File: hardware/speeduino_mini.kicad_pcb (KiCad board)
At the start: 2 copper layers, 264.2 x 66 mm, 209 parts, among them J1 O2, J10 Injector, J11 Ignitor Pack, J12 oil pressure, J13 fuel pressure, J14 power, J15 Conn_01x08_Female, J2 Raspberry_Pi_2_3, J3 TPS, J4 IAT, J5 head temperature, J6 crankshaft position sensor, J7 Injector, J8 Injector, J9 Injector, Q1 2N7002, Q2 SQ3457EV, Q3 2N7002, Q5 SQ3457EV, U10 SN74LVC2T45MDCTTEP, U11 TLE8366, U12 LD1117S50TR_SOT223, U13 DRV103H, U14 DRV103H, U15 DRV103H, U3 ATmega2561-16AU, U4 MPX4250AP1, U5 SN74LVC2T45MDCTTEP, U7 DRV103H, U8 MCP2003B, U9 SN74LVC2T45MDCTTEP, Y1 CSTCE16M0V53-R0

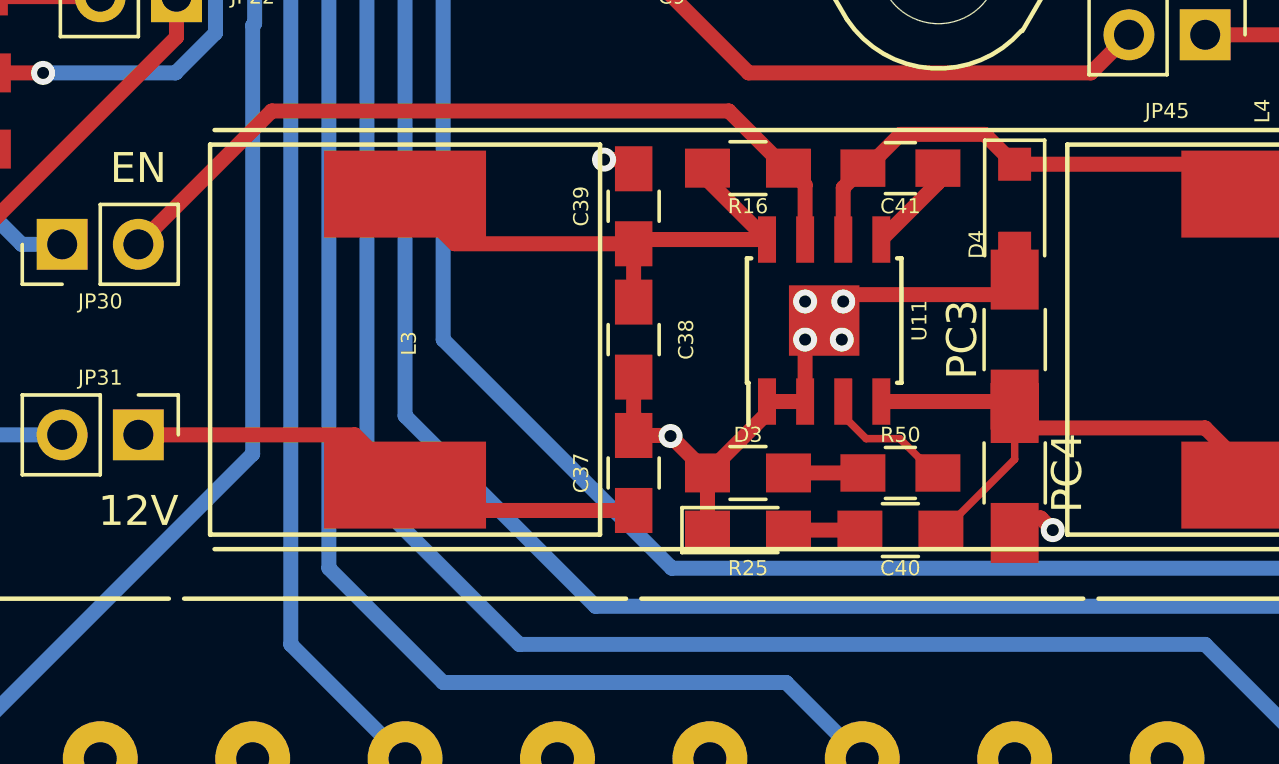
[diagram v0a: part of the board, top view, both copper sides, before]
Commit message: Moved PC3, fixed R25, D3, C40 and R50 silkscreen
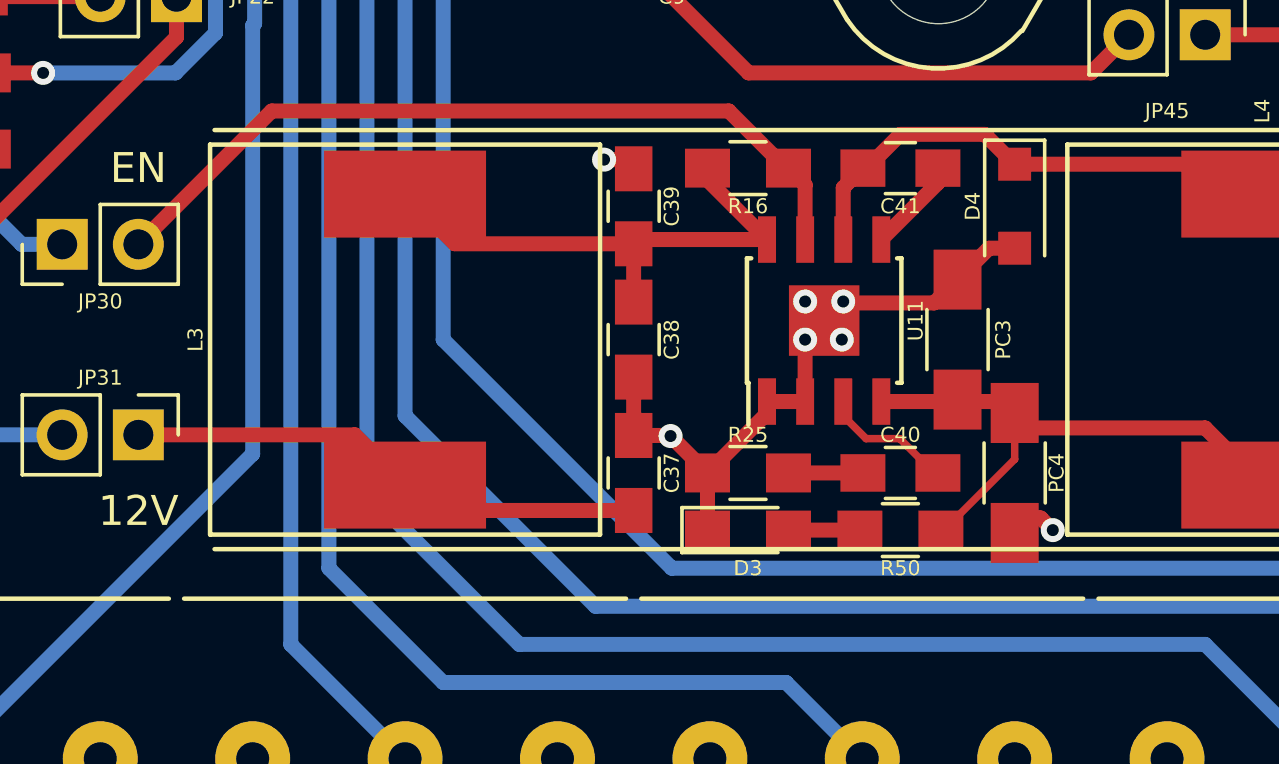
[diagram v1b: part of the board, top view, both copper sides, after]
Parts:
- moved PC3 1.91 mm to (187.3, 108.0)
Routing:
- net GND: track 329.9 -> 329.3 mm
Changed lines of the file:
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@@
     (thickness 1.6)
     (drawings 103)
-    (tracks 1155)
+    (tracks 1156)
     (zones 0)
     (modules 209)
@@
     (tags "capacitor 1206")
     (attr smd)
-    (fp_text reference PC4 (at 0 -1.75 270) (layer F.SilkS)
-      (effects (font (size 1 1) (thickness 0.15)))
+    (fp_text reference PC4 (at 0 -1.397 270) (layer F.SilkS)
+      (effects (font (size 0.5 0.5) (thickness 0.075)))
     )
     (fp_text value "47uF 10V" (at 0 2 270) (layer F.Fab)
@@
   )
   (module Capacitors_SMD:C_1206_HandSoldering (layer F.Cu)
-    (at 189.23 107.95 90)
+    (at 187.325 107.95 90)
     (descr "Capacitor SMD 1206, hand soldering")
     (tags "capacitor 1206")
     (attr smd)
-    (fp_text reference PC3 (at 0 -1.75 90) (layer F.SilkS)
-      (effects (font (size 1 1) (thickness 0.15)))
+    (fp_text reference PC3 (at 0 1.524 90) (layer F.SilkS)
+      (effects (font (size 0.5 0.5) (thickness 0.075)))
     )
     (fp_text value "47uF 10V" (at 0 2 90) (layer F.Fab)
@@
     (tags "SOIC 1.27")
     (attr smd)
-    (fp_text reference U11 (at 0 3.175 90) (layer F.SilkS)
+    (fp_text reference U11 (at 0 3.048 90) (layer F.SilkS)
       (effects (font (size 0.5 0.5) (thickness 0.075)))
     )
@@
     (tags "capacitor 0805")
     (attr smd)
-    (fp_text reference C38 (at 0 -1.75 270) (layer F.SilkS)
+    (fp_text reference C38 (at 0 -1.27 270) (layer F.SilkS)
       (effects (font (size 0.5 0.5) (thickness 0.075)))
     )
@@
     (tags "resistor 0805")
     (attr smd)
-    (fp_text reference R50 (at 0 -3.175) (layer F.SilkS)
+    (fp_text reference R50 (at 0 1.27) (layer F.SilkS)
       (effects (font (size 0.5 0.5) (thickness 0.075)))
     )
@@
     (tags "resistor 0805")
     (attr smd)
-    (fp_text reference D3 (at 0 -3.175) (layer F.SilkS)
+    (fp_text reference D3 (at 0 1.27) (layer F.SilkS)
       (effects (font (size 0.5 0.5) (thickness 0.075)))
     )
@@
     (tags "resistor 0805")
     (attr smd)
-    (fp_text reference R25 (at 0 -3.175 180) (layer F.SilkS)
+    (fp_text reference R25 (at 0 1.27 180) (layer F.SilkS)
       (effects (font (size 0.5 0.5) (thickness 0.075)))
     )
@@
     (tags "capacitor 0805")
     (attr smd)
-    (fp_text reference C40 (at 0 -3.175 180) (layer F.SilkS)
+    (fp_text reference C40 (at 0 1.27 180) (layer F.SilkS)
       (effects (font (size 0.5 0.5) (thickness 0.075)))
     )
@@
     (tags "capacitor 0805")
     (attr smd)
-    (fp_text reference C39 (at 0 -1.75 90) (layer F.SilkS)
+    (fp_text reference C39 (at 0 1.27 90) (layer F.SilkS)
       (effects (font (size 0.5 0.5) (thickness 0.075)))
     )
@@
     (tags "capacitor 0805")
     (attr smd)
-    (fp_text reference C37 (at 0 -1.75 90) (layer F.SilkS)
+    (fp_text reference C37 (at 0 1.27 90) (layer F.SilkS)
       (effects (font (size 0.5 0.5) (thickness 0.075)))
     )
@@
   (module "Speeduino Mini:BOURNS_SRR1260" (layer F.Cu)
     (at 168.91 107.95 90)
-    (fp_text reference L3 (at -0.127 0.127 90) (layer F.SilkS)
+    (fp_text reference L3 (at 0 -6.985 90) (layer F.SilkS)
       (effects (font (size 0.5 0.5) (thickness 0.075)))
     )
@@
     (tags D_SOD-123F)
     (attr smd)
-    (fp_text reference D4 (at 1.27 1.27 270) (layer F.SilkS)
+    (fp_text reference D4 (at 0 1.397 270) (layer F.SilkS)
       (effects (font (size 0.5 0.5) (thickness 0.075)))
     )
@@
   (segment (start 62.865 103.9) (end 62.865 104.9475) (width 0.5) (layer F.Cu) (net 1) (status 10))
   (segment (start 176.53 109.2) (end 176.53 111.145) (width 0.5) (layer F.Cu) (net 1) (status 30))
-  (segment (start 189.23 104.905) (end 189.23 106.45) (width 0.5) (layer F.Cu) (net 1) (status 30))
   (segment (start 178.99 114.3) (end 178.99 112.395) (width 0.5) (layer F.Cu) (net 1) (status 30))
   (segment (start 182.245 110.015) (end 180.975 110.015) (width 0.5) (layer F.Cu) (net 1) (status 30))
@@
   (segment (start 176.53 111.145) (end 177.74 111.145) (width 0.5) (layer F.Cu) (net 1) (status 10))
   (segment (start 183.745 106.45) (end 183.515 106.68) (width 0.5) (layer F.Cu) (net 1) (status 30))
-  (segment (start 189.23 106.45) (end 183.745 106.45) (width 0.5) (layer F.Cu) (net 1) (status 30))
   (segment (start 180.975 110.41) (end 178.99 112.395) (width 0.5) (layer F.Cu) (net 1) (status 30))
   (segment (start 180.975 110.015) (end 180.975 110.41) (width 0.5) (layer F.Cu) (net 1) (status 30))
@@
   (segment (start 152.22 99.06) (end 151.025 97.865) (width 0.5) (layer F.Cu) (net 1) (status 10))
   (segment (start 152.32 99.06) (end 152.22 99.06) (width 0.5) (layer F.Cu) (net 1) (status 30))
+  (segment (start 188.37 104.905) (end 187.325 105.95) (width 0.5) (layer F.Cu) (net 1))
+  (segment (start 189.23 104.905) (end 188.37 104.905) (width 0.5) (layer F.Cu) (net 1))
+  (segment (start 186.5475 106.7275) (end 187.325 105.95) (width 0.5) (layer F.Cu) (net 1))
+  (segment (start 183.4675 106.7275) (end 186.5475 106.7275) (width 0.5) (layer F.Cu) (net 1))
   (segment (start 194.31 124.46) (end 194.31 121.92) (width 0.5) (layer F.Cu) (net 2) (status 20))
   (segment (start 222.25 115.61) (end 222.25 124.46) (width 0.5) (layer F.Cu) (net 2))
@@
   (segment (start 184.785 110.015) (end 189.07 110.015) (width 0.5) (layer F.Cu) (net 106) (status 30))
   (segment (start 189.07 110.015) (end 189.23 109.855) (width 0.5) (layer F.Cu) (net 106) (status 30))
-  (segment (start 189.23 109.45) (end 189.23 109.855) (width 0.5) (layer F.Cu) (net 106) (status 30))
   (segment (start 189.23 109.855) (end 189.23 110.895) (width 0.5) (layer F.Cu) (net 106) (status 30))
   (segment (start 189.23 111.94) (end 189.23 110.895) (width 0.25) (layer F.Cu) (net 106) (status 20))
